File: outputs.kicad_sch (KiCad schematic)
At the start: 42 parts, among them Q1 SQ2362CES, Q3 SQ2362CES, Q6 SQ2362CES, Q7 SQ2362CES, U2 LM393

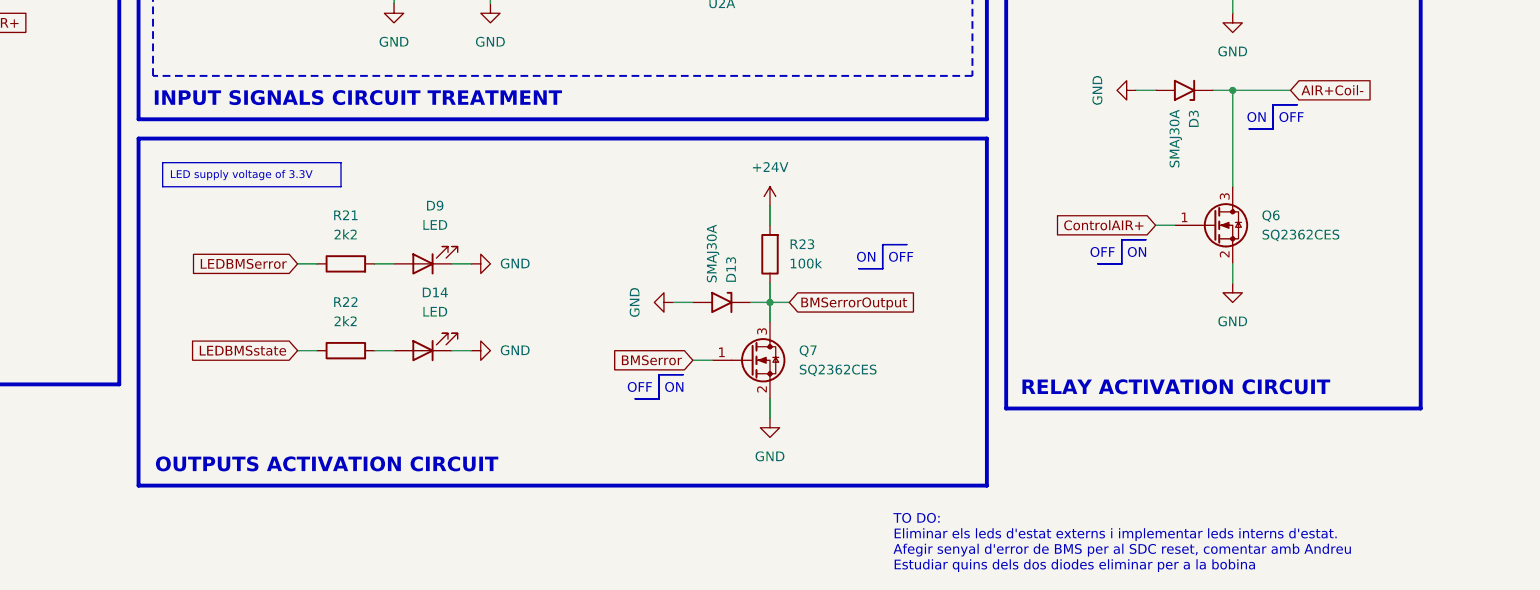
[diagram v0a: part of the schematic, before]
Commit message: Footprints corregides
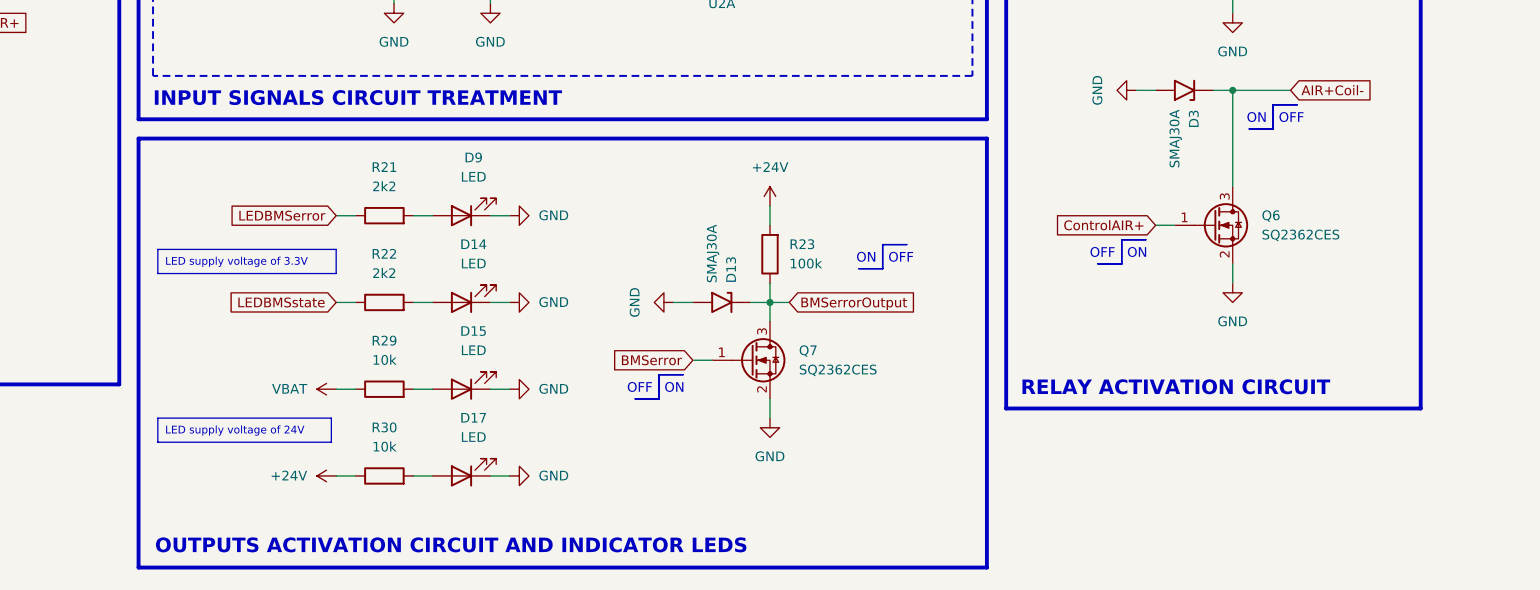
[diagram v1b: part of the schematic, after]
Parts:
- added D15, D17: LED, LED_SMD:LED_0603_1608Metric, symbol Device:LED
- added R29, R30: 10k, Resistor_SMD:R_0603_1608Metric, symbol Device:R
- C12, C13, C14, C15, C27: footprint Capacitor_SMD:C_0603_1608Metric_Pad1.08x0.95mm_HandSolder -> Capacitor_SMD:C_0603_1608Metric
- D14, D9: footprint LED_SMD:LED_0603_1608Metric_Pad1.05x0.95mm_HandSolder -> LED_SMD:LED_0603_1608Metric
- F2, F5, F6: footprint Fuse:Fuse_1206_3216Metric_Pad1.42x1.75mm_HandSolder -> Fuse:Fuse_1206_3216Metric
- R1, R5, R7: footprint Resistor_SMD:R_0201_0603Metric_Pad0.64x0.40mm_HandSolderResistor_SMD:R_0201_0603Metric_Pad0.64x0.40mm_HandSolder -> Resistor_SMD:R_0603_1608Metric
- R15, R16, R2, R24, R3, R4, R6, R8, R9: footprint Resistor_SMD:R_0201_0603Metric_Pad0.64x0.40mm_HandSolder -> Resistor_SMD:R_0603_1608Metric
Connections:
- net +24V: now also R30.1
- net GND: now also D15.1 (K), D17.1 (K)
- new net: D17.2 (A), R30.2
- new net: D15.2 (A), R29.2
- new net VBAT: R29.1
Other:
- note added: "OUTPUTS ACTIVATION CIRCUIT AND INDICATOR LEDS"
- note removed: "OUTPUTS ACTIVATION CIRCUIT"
- note removed: "TO DO: Eliminar els leds d'estat externs i implementar leds interns d'estat. Afegir senyal d'error de BMS per al SDC reset, comentar amb Andreu Estudiar quins dels dos diodes eliminar per a la bobina"
- moved on the sheet: D9, R21, R22

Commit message: - Primer placement dels components - Footprint afegit per la bobina - S'han tret els TVS a les entrades dels contactors auxiliars
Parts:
- removed D11, D12, D5: SMBJ3V3, Diode_SMD:D_SMB, symbol Device:D_TVS
- D4, D7, D8: value D_Schottky -> SD103AWS-G3-18; footprint Diode_SMD:D_SMA -> Diode_SMD:D_SOD-323_HandSoldering; Part Number (none) -> SD103AWS-G3-18

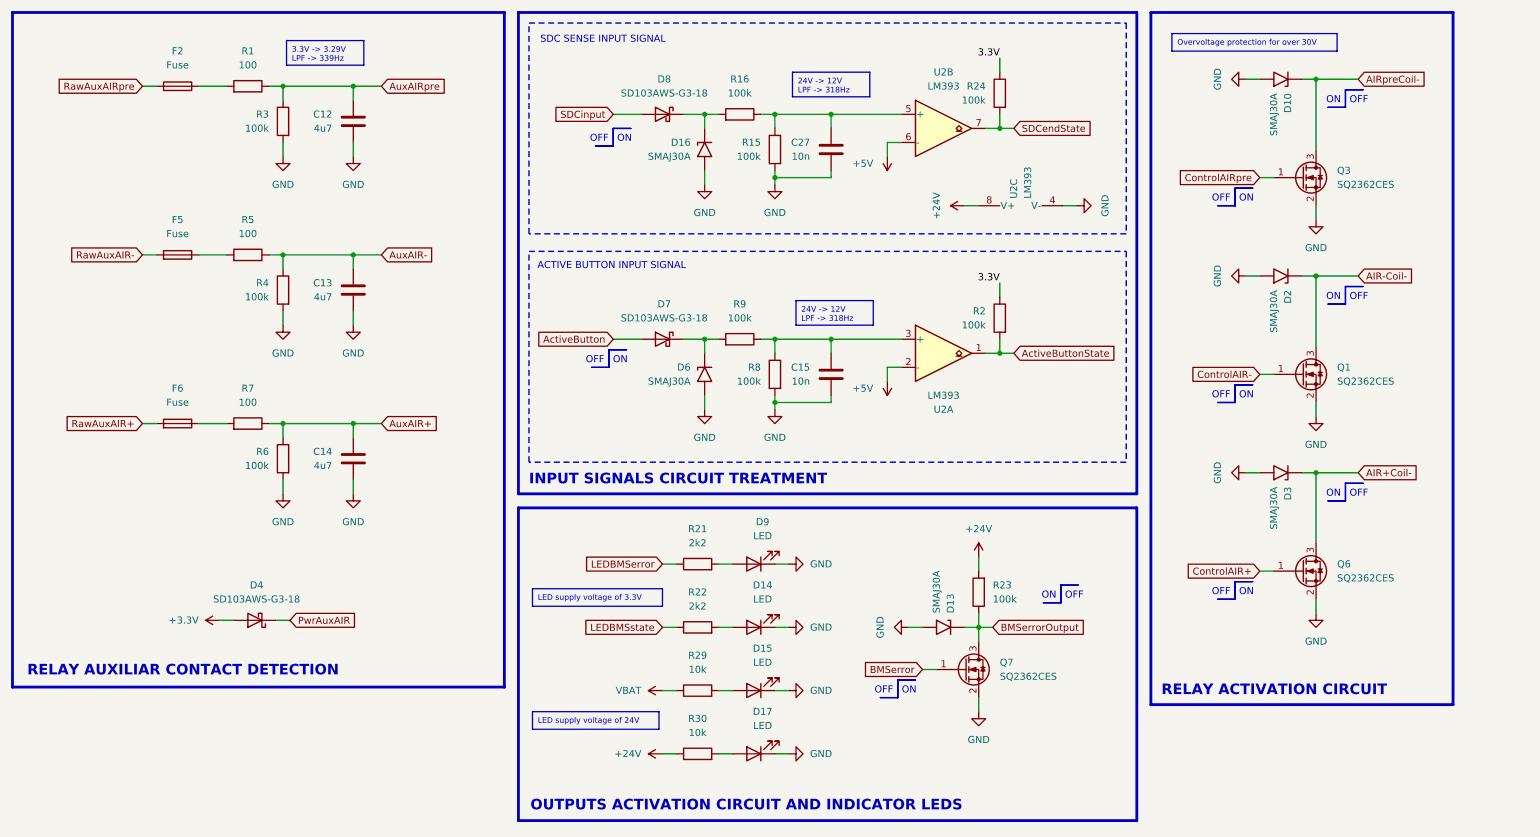
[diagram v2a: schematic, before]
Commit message: - S'han definit tots els parts numbers de R,C i D ajustant a voltatges i potències - Connectors 02x02 canviats a top2bottom - Modificació de l'error de BMS amb sortida open collector - LED blau afegit per saber l'estat de SDC
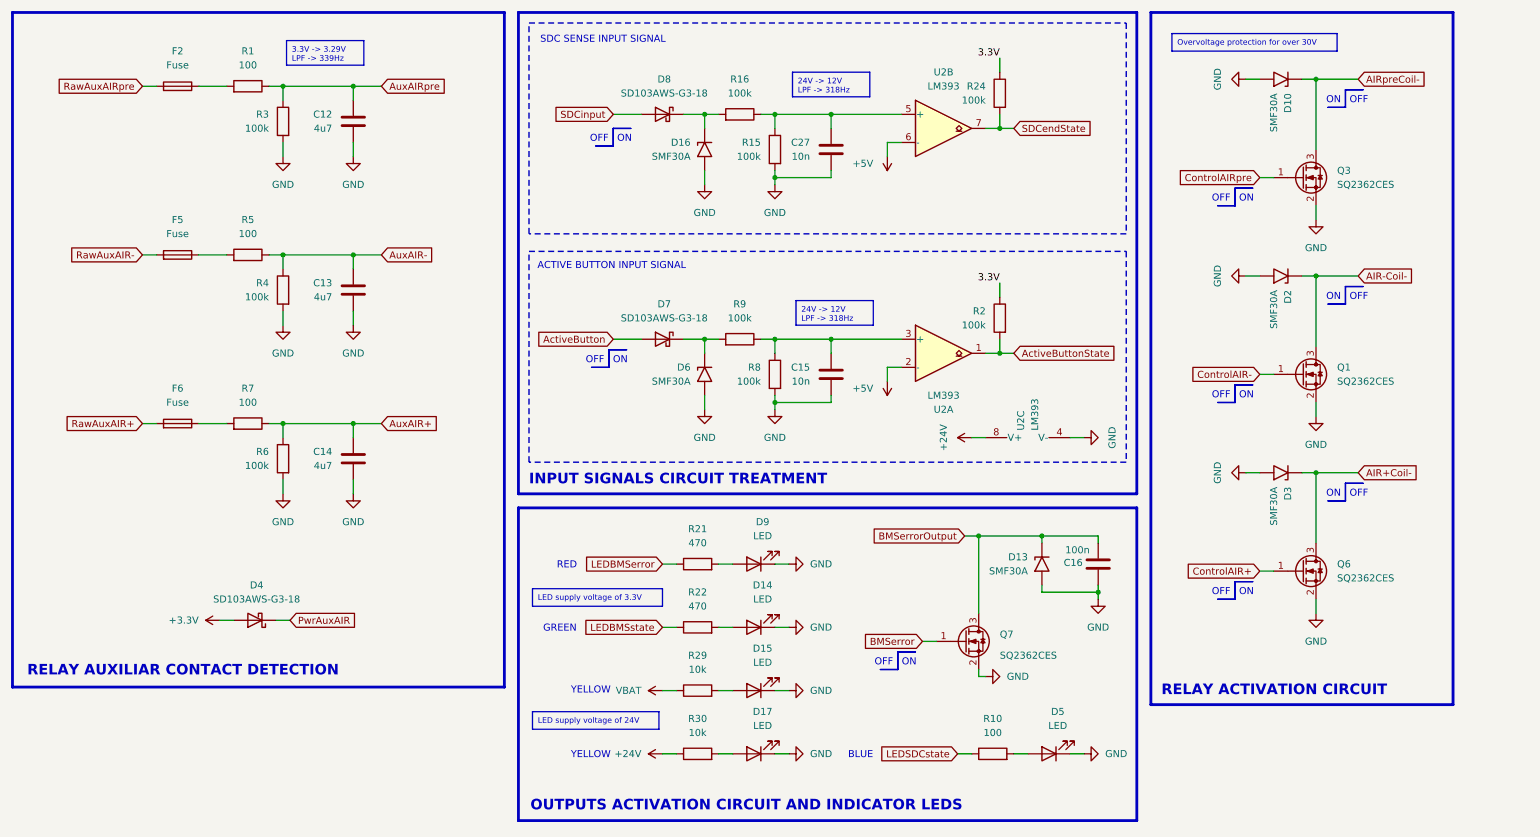
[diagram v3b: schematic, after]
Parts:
- removed R23: 100k, Resistor_SMD:R_0603_1608Metric, symbol Device:R
- added C16: 100n, Capacitor_SMD:C_0603_1608Metric, symbol Device:C
- added D5: LED, LED_SMD:LED_0603_1608Metric, symbol Device:LED
- added R10: 100, Resistor_SMD:R_0603_1608Metric, symbol Device:R
- C12, C13, C14: Part Number (none) -> VJ0603G475KXJCW1BC
- C15, C27: Part Number (none) -> VJ0603Y103KXXCW1BC
- D10, D13, D16, D2, D3, D6: value SMAJ30A -> SMF30A; footprint Diode_SMD:D_SMA -> Diode_SMD:D_SMF; Part Number (none) -> SMF30A
- D14: Part Number (none) -> VLMG1300-GS08
- D15, D17: Part Number (none) -> VLMY1300-GS08
- D9: Part Number (none) -> VLMS1300-GS08
- F2, F5, F6: Part Number (none) -> JB12S5000R
- Q1, Q3, Q6, Q7: Part Number (none) -> SQ2362CES-T1_GE3
- R1, R5, R7: Part Number (none) -> TNPW0603100RBEEA
- R15, R16, R2, R24, R3, R4, R6, R8, R9: Part Number (none) -> TNPW0603100KBEEA
- R21, R22: value 2k2 -> 470; Part Number (none) -> TNPW0603470RBEEA
- R29, R30: Part Number (none) -> CRCW060310K0FKTAHP
- U2: Part Number (none) -> LM393APWR
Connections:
- net BMSerrorOutput: now also C16.2
- net GND: now also C16.1, D5.1 (K)
- new net: D5.2 (A), R10.2
- new net LEDSDCstate: R10.1
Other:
- note added: "BLUE"
- note added: "GREEN"
- note added: "RED"
- note added: "YELLOW"
- moved on the sheet: D13, Q7, U2C

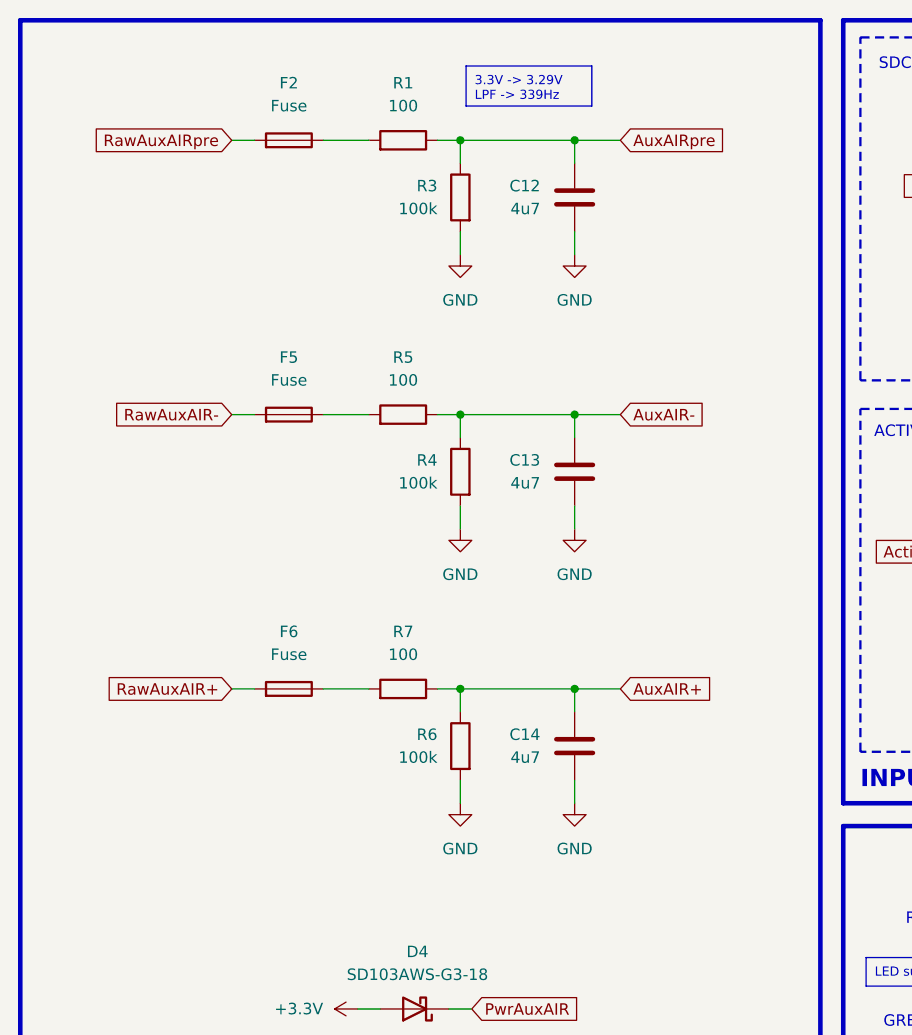
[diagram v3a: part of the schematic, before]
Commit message: Fusibles eliminats de la mesura dels contactors auxiliars Canvi de lloc dels enables del CAN Emplaçament dels inputs, CAN i LEDs al Layout
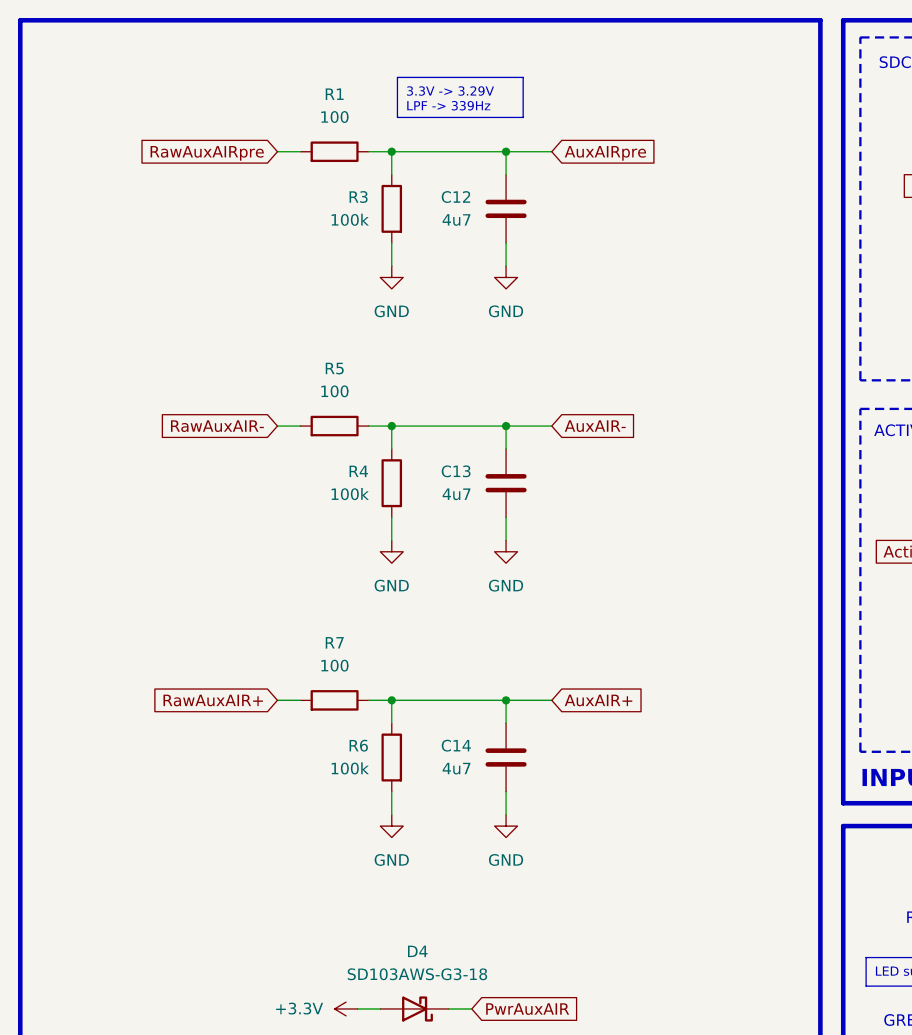
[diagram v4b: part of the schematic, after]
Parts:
- removed F2, F5, F6: Fuse, Fuse:Fuse_1206_3216Metric, symbol Device:Fuse
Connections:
- net RawAuxAIR+: now also R7.2
- net RawAuxAIR-: now also R5.2
- net RawAuxAIRpre: now also R1.2
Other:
- moved on the sheet: C12, C13, C14, R1, R3, R4, R5, R6, R7

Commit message: Layout acabat amb components, pistes i serigrafia completa
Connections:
- net 3.3V is gone; now on net +3.3V: R2.1, R24.1
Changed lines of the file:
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@@
 		)
 	)
-	(label "3.3V"
-		(at 199.39 66.04 180)
-		(effects
-			(font
-				(size 1.27 1.27)
-			)
-			(justify right bottom)
-		)
-	)
-	(label "3.3V"
-		(at 199.39 25.4 180)
-		(effects
-			(font
-				(size 1.27 1.27)
-			)
-			(justify right bottom)
-		)
-	)
 	(global_label "BMSerror"
 		(shape input)
@@
 	)
 	(symbol
+		(lib_id "power:+3.3V")
+		(at 199.39 66.04 90)
+		(unit 1)
+		(body_style 1)
+		(exclude_from_sim no)
+		(in_bom yes)
+		(on_board yes)
+		(in_pos_files yes)
+		(dnp no)
+		(fields_autoplaced yes)
+		(property "Reference" "#PWR039"
+			(at 203.2 66.04 0)
+			(hide yes)
+			(show_name no)
+			(do_not_autoplace no)
+			(effects
+				(font
+					(size 1.27 1.27)
+				)
+			)
+		)
+		(property "Value" "+3.3V"
+			(at 195.58 66.0399 90)
+			(show_name no)
+			(do_not_autoplace no)
+			(effects
+				(font
+					(size 1.27 1.27)
+				)
+				(justify left)
+			)
+		)
+		(property "Footprint" ""
+			(at 199.39 66.04 0)
+			(hide yes)
+			(show_name no)
+			(do_not_autoplace no)
+			(effects
+				(font
+					(size 1.27 1.27)
+				)
+			)
+		)
+		(property "Datasheet" ""
+			(at 199.39 66.04 0)
+			(hide yes)
+			(show_name no)
+			(do_not_autoplace no)
+			(effects
+				(font
+					(size 1.27 1.27)
+				)
+			)
+		)
+		(property "Description" "Power symbol creates a global label with name \"+3.3V\""
+			(at 199.39 66.04 0)
+			(hide yes)
+			(show_name no)
+			(do_not_autoplace no)
+			(effects
+				(font
+					(size 1.27 1.27)
+				)
+			)
+		)
+		(pin "1"
+		)
+		(instances
+			(project "ES_BMU_HW"
+				(path "/241310d7-2595-46fd-a468-4bac14ba2b52/0534aeae-6f70-40f7-b035-12d510ac20ae"
+					(reference "#PWR039")
+					(unit 1)
+				)
+			)
+		)
+	)
+	(symbol
 		(lib_id "power:GND")
 		(at 74.93 105.41 0)
@@
 					(unit 1)
 				)
+			)
+		)
+	)
+	(symbol
+		(lib_id "power:+3.3V")
+		(at 199.39 25.4 90)
+		(unit 1)
+		(body_style 1)
+		(exclude_from_sim no)
+		(in_bom yes)
+		(on_board yes)
+		(in_pos_files yes)
+		(dnp no)
+		(fields_autoplaced yes)
+		(property "Reference" "#PWR038"
+			(at 203.2 25.4 0)
+			(hide yes)
+			(show_name no)
+			(do_not_autoplace no)
+			(effects
+				(font
+					(size 1.27 1.27)
+				)
+			)
+		)
+		(property "Value" "+3.3V"
+			(at 195.58 25.3999 90)
+			(show_name no)
+			(do_not_autoplace no)
+			(effects
+				(font
+					(size 1.27 1.27)
+				)
+				(justify left)
+			)
+		)
+		(property "Footprint" ""
+			(at 199.39 25.4 0)
+			(hide yes)
+			(show_name no)
+			(do_not_autoplace no)
+			(effects
+				(font
+					(size 1.27 1.27)
+				)
+			)
+		)
+		(property "Datasheet" ""
+			(at 199.39 25.4 0)
+			(hide yes)
+			(show_name no)
+			(do_not_autoplace no)
+			(effects
+				(font
+					(size 1.27 1.27)
+				)
+			)
+		)
+		(property "Description" "Power symbol creates a global label with name \"+3.3V\""
+			(at 199.39 25.4 0)
+			(hide yes)
+			(show_name no)
+			(do_not_autoplace no)
+			(effects
+				(font
+					(size 1.27 1.27)
+				)
+			)
+		)
+		(pin "1"
+		)
+		(instances
+			(project "ES_BMU_HW"
+				(path "/241310d7-2595-46fd-a468-4bac14ba2b52/0534aeae-6f70-40f7-b035-12d510ac20ae"
+					(reference "#PWR038")
+					(unit 1)
+				)

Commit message: updated schematics template
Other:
- company: (none) -> EUSS Motorsport
- title: (none) -> BMU
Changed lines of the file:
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@@
 	(generator_version "10.0")
 	(paper "A4")
+	(title_block
+		(title "BMU")
+		(date "2026-10-26")
+		(rev "1.0")
+		(company "EUSS Motorsport")
+		(comment 1 "Martí Xuclà Pinyol")
+	)
 	(rectangle
 		(start 125.603 81.28)
